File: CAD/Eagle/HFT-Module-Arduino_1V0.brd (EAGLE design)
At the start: 96.5 x 96.5 mm, 402 parts, among them Q0521 ABS07-32.768KHZ, Q0811 ABM03B-32.000MHZ, Q0911 ABM3B-16MHZ-10-R50-1-U, T1201 MMBT2222, T1202 MMBT2222, T1203 MMBT2222, U0111 STM32L4Z_144PIN_SMPS, U0431 PAM2305AAB120, U0601 LM4120IM5-3.0, U0611 MAX5217, U0631 CFPT-141-20MHZ, U0641 OPA354, U0701 Si5338, U0801 SX1276, U0901 AX5243, U0911 PE4259, U0921 PE4259, U0991 PE4259, U1101 MCP3911A0-E-SS, U1111 MAX5136AGTG+, U1121 OPA354, U1131 OPA354, U1141 OPA354, U1201 NHD-C0220BIZ_2X20CHARS, U1301 MPU-9250, U1311 MS5607-02BA03, U1321 SHT31-DIS, U1401 SOLARPANEL_3V3_5MA1_25MM_X_20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, U1402 SPV1040T, U1501 TS5A23166, U1601 SC189ZSKTRT, U1701 TS5A23166, U1801 TS5A23166, U1901 TS5A23166, X1261 TTE_EN11-HSM, X2001 MOLEX 105017-0001, X2101 SMA_SMT_AMPHENOL-901-143, SAM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, X2111 SMA_SMT_AMPHENOL-901-143, SAM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, X2201 CUI SJ1-3535NS, X2211 CUI SJ1-3535NS, X2311 2X20/90_1MM27_HARWIN_M50-3202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, X2312 2X20/90_1MM27_HARWIN_M50-3202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, X2321 2X20/90_1MM27_HARWIN_M50-3202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, X2322 2X20/90_1MM27_HARWIN_M50-3202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, X2331 2X20/90_1MM27_HARWIN_M50-3202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, X2332 2X20/90_1MM27_HARWIN_M50-3202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

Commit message: HW_1V0 - Initial setup of PCB
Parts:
- removed C0313, C0421, C0422, C0432, C0441, C0601, C0611, C0612, C0631, C0641, C0701, C0702, C0703, C0705, C1001, C1002, C1003, C1101, C1102, C1103, C1111, C1112, C1231, C1301, C1303, C1311, C1321, C1402, C1403, C1501, C1605, C1701, C1703, C1801, C1803, C1901, C1902, C1903, C1908, C1909: 100nF, rcl:C0603
- removed C0401, C0402, C0403, C0404, C0405, C0406, C0407, C0408, C0409, C0802, C0803, C0804, C0805, C0806, C0807: 100n, rcl:C0603
- removed C0410, C0423: 4.7uF, rcl:C0805
- removed C0412, C0715, C0716, C1302: 10nF, rcl:C0603
- removed C0413, C0442, C0622, C1211, C1221: 1uF, rcl:C0805
- removed C0431, C0444, C1401, C1404: 10uF, rcl:C0805
- removed C0451, C1601, C1607: 1F_EEC-S5R5H105N, df4iah_rcl:W14MM_D8MM_P13MM5
- removed C0511, C0861: 1.5pF, rcl:C0603
- removed C0531: TZY2Z100AC01R00, df4iah_c-trimm:3MM2_X_2MM5
- removed C0632: 100pF, rcl:C0603
- removed C0704: 220nF, rcl:C0603
- removed C0801: 1u, rcl:C0603
- removed C0811: 4.7p, df4iah_c-trimm:3MM2_X_2MM5
- removed C0812: 4.7p, rcl:C0603
- removed C0841, C0850, C0858, C0872, C_AX_C1, C_AX_C2, C_AX_M2: 0pF, rcl:C0603
- removed C0843: 3.3pF, rcl:C0603
- removed C0844, C0846, C0851, C0852, C0873, C0875, C1113: 47pF, rcl:C0603
- removed C0853, C0863, C0871, C_AX_A2, C_AX_A3, C_AX_B2, C_AX_F2, C_AX_M1: 4.7pF, rcl:C0603
- removed C0854: 15nH, rcl:C0603
- removed C0856, C0859: 6.8pF, rcl:C0603
- removed C0857: 2.7pF, rcl:C0603
- removed C0862: 33pF, rcl:C0603
- removed C0864: 1.2pF, rcl:C0603
- removed C0865: 1.8pF, rcl:C0603
- removed C0911, C0921, C0999, C1261, C1262, C1271: 1nF, rcl:C0603
- removed C0991: 100pF HiQ, rcl:C0603
- removed C0992, C0993: 330pF HiQ, rcl:C0603
- removed C0994, C0996: 0nF HiQ, rcl:C0603
- removed C1104, C1105, C1131, C1141: 220nF, df4iah_rcl:C0603
- removed C1128, C1129: 100nF, df4iah_rcl:C0603
- removed C1132, C1142: 100uF, df4iah_rcl:C0805
- removed C1405: 0nF, rcl:C0603
- removed C1406, C1602, C1606: 47uF, rcl:C0805
- removed C2003: 1nF, df4iah_rcl:C0603
- removed C_AX_T1, C_AX_T2: 4.3pF, rcl:C0603
- removed D0451: CMAD6001, df4iah_diode:SOD923
- removed D1403, D1501: CRS08, df4iah_diode:SOD80C
- removed FM1, FM2, FM3: (no value), df4iah_fiducial:FIDUCIAL_MARK_1MM
- removed H2401, H2404: MOUNT-PAD-ROUND2.8, holes:2,8-PAD
- removed L0411, L1102, L1112: 10uH, rcl:L2012C
- removed L0433: 2.2uH 14mR, df4iah_rcl:L_6X6MM
- removed L0842, L0862: 10nH, rcl:R0603
- removed L0851: 68nH, rcl:R0603
- removed L0856, L0858, L0995, R0201, R0202, R0211, R0212, R0221, R0222, R0231, R0232, R0441, R0612, R0613, R0811, R0845, R0874, R1404, R1405, R1406, R1409: 0R, rcl:R0603
- removed L0857: 12nH, rcl:R0603
- removed L0861: 33nH, rcl:R0603
- removed L0864: 6.2nH, rcl:R0603
- removed L0871: 18nH, rcl:R0603
- removed L1403: 33uH, df4iah_rcl:L_13.5X12.5MM
- removed L1604: 1.0uH 33mR, rcl:L5650M
- removed L_AX_1, L_AX_B1, L_AX_B2, L_AX_F1: 22nH, rcl:R0603
- removed L_AX_C1, L_AX_C2: 100nH, rcl:R0603
- removed L_AX_T1, L_AX_T2: 43nH, rcl:R0603
- removed PF2011: 1.1A/2.2A, rcl:M1206
- removed Q0521: ABS07-32.768KHZ, df4iah_crystal:ABS07
- removed Q0811: ABM03B-32.000MHZ, df4iah_crystal:ABM03B
- removed Q0911: ABM3B-16MHZ-10-R50-1-U, df4iah_crystal:ABM03B
- removed R0241, R0242, R0243, R0251, R0252, R0253, R0254, R0261, R0262, R0263, R0269, R0271, R0272, R0273, R0274, R0275, R0276, R0277, R0281, R0282, R0283, R0284, R0285, R0286, R0287, R0288, R0289, R0290, R0291, R0292, R0293, R0294, R0295, R0296, R0642, R0713, R0714, R0723, R0724, R0731, R0732, R0735, R0736, R0743, R0744, R0802, R0803, R0831, R1021, R1041, R1051, R1061, R1106, R1107, R1108, R1109, R1114, R2310, R2311, R2312, R2313, R2314, R2315, R2316, R2317, R2318, R2320, R2321, R2322, R2323, R2324, R2325, R2326, R2327, R2328, R2330, R2331, R2332, R2333, R2334, R2335, R2336, R2337, R2338: 47R, rcl:R0603
- removed R0311: 3.3kR, rcl:R0603
- removed R0321, R0631, R1131, R1141, R1261, R1262, R1271: 10kR, rcl:R0603
- removed R0611: open, rcl:R0603
- removed R0621, R1031, R1032, R1407, R1412: 100kR, rcl:R0603
- removed R0638, R0639: 50R, rcl:R0603
- removed R0711, R0712: none, rcl:R0603
- removed R0751, R0801, R0821: 100R, rcl:R0603
- removed R0804, R0805, R0806, R0807: NC, rcl:R0603
- removed R1104, R1105: 22kR, rcl:R0603
- removed R1110, R1132, R1135, R1142, R1145, R1241, R1502, R1702, R1802, R1902: 33kR, rcl:R0603
- removed R1201, R1205, R1208: 1.8kR, rcl:R0603
- removed R1202: 5.2kR, rcl:R0603
- removed R1203: 68R, rcl:R0805
- removed R1204, R1207: 2.2kR, rcl:R0603
- removed R1206, R1209: 10R, rcl:R0805
- removed R1301: 68R, rcl:R0603
- removed R1331, R1332: 3.9kR, rcl:R0603
- removed R1408: 310kR, rcl:R0603
- removed R1411: 1kR, rcl:R0603
- removed R2002: 330kR, rcl:R0603
- removed S0312: KSR223G, df4iah_switch:KSR223G_SMD_1POL
- removed SJ0121, SJ0401, SJ0421, SJ0422, SJ0423, SJ0424: (no value), df4iah_jumper:SJ
- removed T1201, T1202, T1203: MMBT2222, transistor:SOT23
- removed TP_+1V2, TP_+1V2_MCU, TP_+3V3, TP_+3V3_20MHZ, TP_+3V3_HICUR, TP_+5V0, TP_+5V0_SOL, TP_+5V0_USB_SW, TP_VBAT, TP_VSOL: PTR1B1,27, testpad:B1,27
- removed TP_AX_ADC1, TP_AX_ADC2, TP_AX_IRQ, TP_AX_TCXO_EN, TP_SX_DIO0, TP_SX_DIO1, TP_SX_DIO2, TP_SX_DIO3, TP_SX_DIO4, TP_SX_DIO5, TP_SX_RXTX: PTR1TP06R, testpad:TP06R
- removed U0111: STM32L4Z_144PIN_SMPS, df4iah_stm32l4:LQFP144
- removed U0431: PAM2305AAB120, df4iah_powersupply:SOT95P280X145-5N
- removed U0601: LM4120IM5-3.0, df4iah_powersupply:SOT95P285X120-5N
- removed U0611: MAX5217, df4iah_dac:µMAX8
- removed U0631: CFPT-141-20MHZ, df4iah_osc:CFPT-141
- removed U0641, U1121, U1131, U1141: OPA354, df4iah_opamp:SOT-23-5
- removed U0701: Si5338, df4iah_osc:QFN24_P0MM5_CTRPAD
- removed U0801: SX1276, df4iah_rf:QFN28-6X6-0P65-PAD
- removed U0901: AX5243, df4iah_rf:QFN20-4X4-0P5-PAD
- removed U0911, U0921, U0991: PE4259, df4iah_rf:SC-70_6-LEAD_2X1MM25_0P65
- removed U1101: MCP3911A0-E-SS, df4iah_adc:QFN20_P0MM5_CTRPAD
- removed U1111: MAX5136AGTG+, df4iah_dac:QFN24_P0MM5_CTRPAD
- removed U1201: NHD-C0220BIZ_2X20CHARS, df4iah_lcd:NHD-C0220BIZ_2X20CHARS
- removed U1301: MPU-9250, df4iah_sensors:QFN24-3X3
- removed U1311: MS5607-02BA03, df4iah_sensors:MS5607-02BA
- removed U1321: SHT31-DIS, df4iah_sensors:DFN8/SHT
- removed U1401: SOLARPANEL_3V3_5MA1_25MM_X_20MM, df4iah_supply:SOLARPANEL_3V3_5MA1_25MM_X_20MM
- removed U1402: SPV1040T, df4iah_powersupply:TSSOP8
- removed U1501, U1701, U1801, U1901: TS5A23166, df4iah_sc-switches:R-PDSO-G8
- removed U1601: SC189ZSKTRT, df4iah_powersupply:SOT95P280X145-5N
- removed X0301: (no value), df4iah_connector:2X03
- removed X0322: (no value), df4iah_connector:1X02
- removed X1261: TTE_EN11-HSM, df4iah_switch:TTE_EN11-HSM
- removed X2001: MOLEX 105017-0001, df4iah_connector:USB-B-MICRO-SMD_MOLEX-105017-0001
- removed X2101, X2111: SMA_SMT_AMPHENOL-901-143, SAMTEC SMA-J-P-H-RA-TH1, df4iah_connector:SMA_SMT_AMPHENOL_901-143
- removed X2201, X2211: CUI SJ1-3535NS, df4iah_connector:SJ1-353XNS_3MM5-STEREO-AUDIO-JACKS
- removed X2311, X2312, X2321, X2322, X2331, X2332: 2X20/90_1MM27_HARWIN_M50-3202045, df4iah_connector:2X20/90_1MM27_HARWIN_M50-3202045
- added R111, R112, R113, R114, R115, R121, R122, R123, R124: 47R, rcl:R0603
- added X111, X121: 2X20/90_1MM27_HARWIN_M50-3202045, df4iah_connector:2X20/90_1MM27_HARWIN_M50-3202045
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- renumbered H2402 to H412, H2403 to H411
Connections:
- removed net +1V2: C0444.1, C1901.1, L0433.1, TP_+1V2.TP, U0431.4, U1901.1, U1901.5
- removed net +1V5_UNUSED: SJ0424.2
- removed net +1V8_UNUSED: SJ0423.2
- removed net +2V5_UNUSED: SJ0422.2
- removed net +3V0_20MHZ_VCTCXO: C0611.1, C0631.1, U0601.5, U0611.1, U0631.4
- removed net +3V3_20MHZ: C0612.1, C0641.1, C1803.1, R0611.1, R0613.1, TP_+3V3_20MHZ.TP, U0611.7, U0641.5, U1801.2, U1801.6
- removed net +3V3_HICUR: C0701.1, C0702.1, C0703.1, C0704.1, C0705.2, C1101.1, C1111.1, C1128.1, C1129.1, C1703.1, L1102.2, L1112.2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
- removed net +5V1_SOL: C1406.1, R1405.2, R1406.2, R1408.2, R1409.1, TP_+5V0_SOL.TP
- removed net 20MHZ_DAC_OUT: R0621.1, U0611.6
- removed net 20MHZ_XO: R0638.1, U0631.3
- removed net 20MHZ_XON: C0716.1, R0639.2, R0751.1
- removed net 20MHZ_XOP: C0715.1, R0638.2, R0751.2
- removed net AD_VCTCXO1: R0642.1, U0641.1, U0641.4
- removed net AUDIO_IN_L: C1104.1, X2201.2
- removed net AUDIO_IN_R: C1105.1, X2201.3
- removed net AUDIO_OUT_L: C1132.2, X2211.2
- removed net AUDIO_OUT_L_OP: C1132.1, U1131.1, U1131.4
- removed net AUDIO_OUT_R: C1142.2, X2211.3
- removed net AUDIO_OUT_R_OP: C1142.1, U1141.1, U1141.4
- removed net AX_16MHZ: R0714.1, R1021.2
- removed net AX_ADC1: R1031.1, TP_AX_ADC1.TP, U0901.17
- removed net AX_ADC2: R1032.1, TP_AX_ADC2.TP, U0901.18
- removed net AX_ANTN: C_AX_C2.1, C_AX_T2.1, L_AX_C2.1, U0901.4
- removed net AX_ANTP: C_AX_C1.1, C_AX_T1.1, L_AX_C1.1, U0901.3
- removed net AX_B1: C_AX_M1.1, L_AX_B1.1, L_AX_T1.2
- removed net AX_B2: C_AX_B2.1, C_AX_M2.1, L_AX_B2.2, L_AX_T2.2
- removed net AX_CLK16N: Q0911.1, U0901.19
- removed net AX_CLK16P: Q0911.3, U0901.20
- removed net AX_COMB: C_AX_A2.1, C_AX_B2.2, C_AX_F2.1, L_AX_B1.2, L_AX_F1.1
- removed net AX_GPIO1: R1061.2, TP_AX_TCXO_EN.TP, U0901.15
- removed net AX_IRQ: R1051.2, TP_AX_IRQ.TP, U0901.14
- removed net AX_L1: L_AX_1.1, U0901.8
- removed net AX_L2: L_AX_1.2, U0901.7
- removed net AX_SYSCLK: R1021.1, U0901.9
- removed net AX_T1: C_AX_T1.2, L_AX_T1.1
- removed net AX_T2: C_AX_T2.2, L_AX_T2.1
- removed net AX_VDD1: C1002.2, U0901.1
- removed net AX_VDD5: C1003.2, U0901.5
- removed net CH1_ANT: C0996.1, L0995.2, X2101.1
- removed net CH2_ANT: C_AX_A3.1, C_AX_F2.2, L_AX_F1.2, X2111.1
- removed net CLK0_N: R0743.2, X2332.4
- removed net CLK0_P: R0744.2, X2332.3
- removed net CLK1_N: R0735.2, X2322.4
- removed net CLK1_P: R0736.2, X2322.3
- removed net CLK2_N: R0731.2, X2312.4
- removed net CLK2_P: R0732.2, X2312.3
- removed net EVT_N: R2314.2, X2311.29
- removed net EVT_S: R2334.2, X2331.29
- removed net EVT_W: R2324.2, X2321.29
- removed net I2S_FS_IN_N: R2317.2, X2312.26
- removed net I2S_FS_IN_S: R2337.2, X2332.26
- removed net I2S_FS_IN_W: R2327.2, X2322.26
- removed net I2S_FS_OUT: R0284.2, X2312.20, X2322.20, X2332.20
- removed net I2S_MCLK_OUT: R0283.2, X2312.19, X2322.19, X2332.19
- removed net I2S_SCK_IN_N: R2315.2, X2312.23
- removed net I2S_SCK_IN_S: R2335.2, X2332.23
- removed net I2S_SCK_IN_W: R2325.2, X2322.23
- removed net I2S_SCK_OUT: R0281.2, X2312.17, X2322.17, X2332.17
- removed net I2S_SD_IN_N: R2316.2, X2312.24
- removed net I2S_SD_IN_S: R2336.2, X2332.24
- removed net I2S_SD_IN_W: R2326.2, X2322.24
- removed net I2S_SD_OUT: R0282.2, X2312.18, X2322.18, X2332.18
- removed net LCD_C1+: C1211.2, U1201.7
- removed net LCD_C1-: C1211.1, U1201.8
- removed net LCD_VOUT: C1221.1, U1201.6
- removed net LED_B_B: R1207.1, R1208.2, T1203.1
- removed net LED_B_E: R1209.2, T1203.2
- removed net LED_B_K: T1203.3, U1201.11
- removed net LED_G_B: R1204.1, R1205.2, T1202.1
- removed net LED_G_E: R1206.2, T1202.2
- removed net LED_G_K: T1202.3, U1201.10
- removed net LED_R_B: R1201.1, R1202.2, T1201.1
- removed net LED_R_E: R1203.2, T1201.2
- removed net LED_R_K: T1201.3, U1201.9
- removed net MAX5136_!READY: R1114.2, U1111.4
- removed net MAX5136_AVDD: C1112.2, L1112.1, U1111.16, U1111.24
- removed net MAX5136_OUT0: R1131.1, U1111.1
- removed net MAX5136_OUT0_R: C1131.1, R1131.2
- removed net MAX5136_OUT0_SUM: C1131.2, R1132.2, R1135.2, U1131.3
- removed net MAX5136_OUT1: R1141.1, U1111.18
- removed net MAX5136_OUT1_R: C1141.1, R1141.2
- removed net MAX5136_OUT1_SUM: C1141.2, R1142.2, R1145.2, U1141.3
- removed net MAX5136_REF: C1113.1, U1111.21, U1111.22, U1121.3
- removed net MAX5136_REF_OP: R1132.1, R1142.1, U1121.1, U1121.4
- removed net MAX5217_!AUX: R0613.2, U0611.5
- removed net MAX5217_ADDR: R0611.2, R0612.2, U0611.2
- removed net MCP3911_!DR: R1106.1, U1101.11
- removed net MCP3911_CH0+: C1104.2, R1104.2, U1101.1
- removed net MCP3911_CH1+: C1105.2, R1105.2, U1101.3
- removed net MCP3911_MDAT0: R1108.1, U1101.10
- removed net MCP3911_MDAT1: R1109.1, U1101.9
- removed net MCP3911_REFINOUT: C1103.2, U1101.6
- removed net MCP3911_SDO: R1107.1, U1101.16
- removed net MCU_AX_MISO: R1041.2, U0901.12
- removed net MCU_I2C1_SCL: R0201.2, X2312.7
- removed net MCU_I2C1_SDA: R0202.2, X2312.8
- removed net MCU_I2C2_SCL: R0211.2, X2322.7
- removed net MCU_I2C2_SDA: R0212.2, X2322.8
- removed net MCU_I2C3_SCL: R0221.2, X2332.7
- removed net MCU_I2C3_SDA: R0222.2, X2332.8
- removed net MCU_I2C4_SCL: R0231.2, R1332.1, U0611.3, U0701.12, U1201.2, U1301.23, U1311.8, U1321.4
- removed net MCU_I2C4_SDA: R0232.2, R1331.1, U0611.4, U0701.19, U1201.3, U1301.24, U1311.7, U1321.1
- removed net MCU_MCO: R0271.2, R0713.1
- removed net MCU_NRST: C0313.1, R0311.2, S0312.2, U0111.25
- removed net MCU_OUT_20MHZ_EN: R0273.2, R1802.2, U0601.3, U1801.3, U1801.7
- removed net MCU_OUT_AUDIO_ADC_NRESET: R0261.2, R1110.2, U1101.18
- removed net MCU_OUT_AUDIO_ADC_SEL: R0262.2, U1101.14
- removed net MCU_OUT_AUDIO_DAC_SEL: R0263.2, U1111.10
- removed net MCU_OUT_AX_SEL: R0253.2, U0901.10
- removed net MCU_OUT_HICUR_EN: R0275.2, R1702.2, U1701.3, U1701.7
- removed net MCU_OUT_LCD_NRST: R0272.2, R1241.2, U1201.1
- removed net MCU_OUT_SX_SEL: R0254.2, U0801.19
- removed net MCU_OUT_VDD12_EN: R0276.2, R1902.2, U1901.3, U1901.7
- removed net MCU_OUT_VUSB_EN: R0274.2, R1502.2, U1501.3, U1501.7
- removed net MCU_SPI1_MISO: R0243.2, X2312.12, X2322.12, X2332.12
- removed net MCU_SPI1_MOSI: R0242.2, X2312.11, X2322.11, X2332.11
- removed net MCU_SPI1_SCK: R0241.2, X2312.13, X2322.13, X2332.13
- removed net MCU_SPI3_MOSI: R0252.2, U0801.18, U0901.13, U1101.17, U1111.9
- removed net MCU_SPI3_SCK: R0251.2, U0801.16, U0901.11, U1101.15, U1111.12
- removed net MCU_SX_TX_RX_CTRL: R0277.2, U0991.4
- removed net MCU_VBAT: C0451.+, D0451.C, TP_VBAT.TP, U0111.6
- removed net MCU_VDD: C0401.1, C0402.1, C0403.1, C0404.1, C0405.1, C0406.1, C0407.1, C0408.1, C0409.1, C0410.1, L0411.2, SJ0401.2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
- removed net MCU_VDD12: C1903.1, C1908.2, C1909.1, TP_+1V2_MCU.TP, U0111.142, U0111.70, U1901.2, U1901.6
- removed net MCU_VDDA: C0412.1, C0413.1, L0411.1, U0111.33
- removed net MCU_VDDIO2: C0421.2, C0422.1, C0423.1, SJ0421.1, SJ0422.1, SJ0423.1, SJ0424.1, U0111.131, U0111.95
- removed net MCU_VREF_M: R0441.2, U0111.31
- removed net MCU_VREF_P: C0441.2, C0442.2, U0111.32
- removed net MCU_VSSA: SJ0121.2, U0111.30
- removed net MCU_WAKEUP: R0269.2, X2311.33, X2321.33, X2331.33
- removed net MPU_INT: R1301.1, U1301.12
- removed net MPU_REGOUT: C1303.1, U1301.10
- removed net MVP3911_AVDD: C1102.2, L1102.1, U1101.20
- removed net PA0: R0292.1, U0111.34
- removed net PA1: U0111.35
- removed net PA10: U0111.102, X2001.ID
- removed net PA13: U0111.105, X0301.1
- removed net PA14: U0111.109, X0301.5
- removed net PA15: U0111.110
- removed net PA2: R0289.1, U0111.36
- removed net PA3: R1411.2, U0111.37
- removed net PA4: U0111.40
- removed net PA5: U0111.41
- removed net PA6: R0296.1, U0111.42
- removed net PA7: R1204.2, U0111.43
- removed net PA8: R0271.1, U0111.100
- removed net PA9: PF2011.1, U0111.101, X2001.VBUS
- removed net PA_USB_N: U0111.103, X2001.D-
- removed net PA_USB_P: U0111.104, X2001.D+
- removed net PB0: R1207.2, U0111.46
- removed net PB1: R0295.1, U0111.47
- removed net PB10: R1261.2, U0111.69
- removed net PB12: R1262.2, U0111.73
- removed net PB13: R2315.1, R2325.1, R2335.1, U0111.74
- removed net PB14: R1271.2, U0111.75
- removed net PB15: U0111.76
- removed net PB2: U0111.48
- removed net PB3: R2310.1, U0111.132
- removed net PB4: U0111.133
- removed net PB5: R2311.1, U0111.134
- removed net PB6: R2312.1, U0111.135
- removed net PB7: R2313.1, U0111.136
- removed net PB8: U0111.138
- removed net PB9: U0111.139
- removed net PC0: R0276.1, U0111.26
- removed net PC1: R0275.1, U0111.27
- removed net PC10: R0251.1, U0111.111
- removed net PC11: R0831.1, R1041.1, R1107.2, U0111.112
- removed net PC12: R0252.1, U0111.113
- removed net PC13: R0269.1, U0111.7
- removed net PC14_MCU_OSC32_IN: C0531.-, Q0521.2, U0111.8
- removed net PC15_MCU_OSC32_OUT: C0511.1, Q0521.1, U0111.9
- removed net PC2: R0274.1, U0111.28
- removed net PC3: R0273.1, U0111.29
- removed net PC4: R0293.1, U0111.44
- removed net PC5: R0294.1, U0111.45
- removed net PC6: R1201.2, U0111.96
- removed net PC7: U0111.97
- removed net PC8: R1114.1, U0111.98
- removed net PC9: R0263.1, U0111.99
- removed net PD0: R1109.2, U0111.114
- removed net PD1: R1108.2, U0111.115
- removed net PD10: R2331.1, U0111.79
- removed net PD11: R2316.1, R2326.1, R2336.1, U0111.80
- removed net PD12: R2317.1, R2327.1, R2337.1, U0111.81
- removed net PD13: R0232.1, U0111.82
- removed net PD14: R2332.1, U0111.85
- removed net PD15: R2333.1, U0111.86
- removed net PD2: R1106.2, U0111.116
- removed net PD3: R0261.1, U0111.117
- removed net PD4: R0291.1, U0111.118
- removed net PD5: R0262.1, U0111.119
- removed net PD6: R0290.1, U0111.122
- removed net PD7: U0111.123, U0701.8
- removed net PD8: R0821.1, U0111.77
- removed net PD9: R2330.1, U0111.78
- removed net PE0: R2314.1, U0111.140
- removed net PE1: U0111.141
- removed net PE10: R0283.1, U0111.63
- removed net PE11: R0253.1, U0111.64
- removed net PE12: R0254.1, U0111.65
- removed net PE13: R0241.1, U0111.66
- removed net PE14: R0243.1, U0111.67
- removed net PE15: R0242.1, U0111.68
- removed net PE2: R2323.1, U0111.1
- removed net PE3: R0282.1, U0111.2
- removed net PE4: R2322.1, U0111.3
- removed net PE5: R2321.1, U0111.4
- removed net PE6: U0111.5
- removed net PE7: R1051.1, U0111.58
- removed net PE8: R0281.1, U0111.59
- removed net PE9: R0284.1, U0111.60
- removed net PF0: R0212.1, U0111.10
- removed net PF1: R0211.1, U0111.11
- removed net PF10: R2324.1, U0111.22
- removed net PF11: U0111.49
- removed net PF12: R0272.1, U0111.50
- removed net PF13: R1301.2, U0111.53
- removed net PF14: R0231.1, U0111.54
- removed net PF15: U0111.55
- removed net PF2: R2320.1, U0111.12
- removed net PF3: R0642.2, U0111.13
- removed net PF4: U0111.14
- removed net PF5: U0111.15
- removed net PF6: R2318.1, U0111.18
- removed net PF7: R2328.1, U0111.19
- removed net PF8: R2338.1, U0111.20
- removed net PF9: R1412.1, U0111.21
- removed net PG0: R0277.1, U0111.56
- removed net PG1: R1061.1, U0111.57
- removed net PG10: R0286.1, U0111.125
- removed net PG11: R0288.1, U0111.126
- removed net PG12: R0287.1, U0111.127
- removed net PG13: R0202.1, U0111.128
- removed net PG14: R0201.1, U0111.129
- removed net PG2: R0802.2, U0111.87
- removed net PG3: R0803.2, U0111.88
- removed net PG4: R2334.1, U0111.89
- removed net PG5: U0111.90
- removed net PG6: U0111.91
- removed net PG7: R0221.1, U0111.92
- removed net PG8: R0222.1, U0111.93
- removed net PG9: R0285.1, U0111.124
- removed net PH0: R0724.1, U0111.23
- removed net PH1: U0111.24
- removed net PH3_BOOT0: R0321.2, U0111.137, X0322.1
- removed net PN00: R2310.2, X2311.7
- removed net PN01: R2311.2, X2311.9
- removed net PN02: R2312.2, X2311.11
- removed net PN03: R2313.2, X2311.13
- removed net PS00: R2330.2, X2331.7
- removed net PS01: R2331.2, X2331.9
- removed net PS02: R2332.2, X2331.11
- removed net PS03: R2333.2, X2331.13
- removed net PW00: R2320.2, X2321.7
- removed net PW01: R2321.2, X2321.9
- removed net PW02: R2322.2, X2321.11
- removed net PW03: R2323.2, X2321.13
- removed net ROTENC_A: C1261.1, R1261.1, X1261.A
- removed net ROTENC_B: C1262.1, R1262.1, X1261.B
- removed net ROTENC_E: C1271.1, R1271.1, X1261.E
- removed net SI5338_CLK0A: R0744.1, U0701.22
- removed net SI5338_CLK0B: R0743.1, U0701.21
- removed net SI5338_CLK1A: R0736.1, U0701.18
- removed net SI5338_CLK1B: R0735.1, U0701.17
- removed net SI5338_CLK2A: R0732.1, U0701.14
- removed net SI5338_CLK2B: R0731.1, U0701.13
- removed net SI5338_CLK3A: R0724.2, U0701.10
- removed net SI5338_CLK3B: R0723.2, U0701.9
- removed net SI5338_CLK3B_2: R0723.1, U1101.12
- removed net SI5338_IN1: R0711.2, U0701.1
- removed net SI5338_IN2: R0712.2, U0701.2
- removed net SI5338_IN3: R0713.2, U0701.3
- removed net SI5338_IN4: R0714.2, U0701.4
- removed net SI5338_IN5: C0715.2, U0701.5
- removed net SI5338_IN6: C0716.2, U0701.6
- removed net SI5338_IN_CLK1: R0711.1
- removed net SI5338_IN_CLK2: R0712.1
- removed net SPV_ICTRL_M: C1405.2, R1405.1, U1402.6
- removed net SPV_ICTRL_P: C1405.1, R1404.1, U1402.7
- removed net SPV_LX: D1403.A, L1403.1, R1412.2, U1402.3
- removed net SPV_VCTRL: R1407.2, R1408.1, U1402.5
- removed net SPV_VOUT: C1403.1, C1404.1, D1403.C, R1404.2, R1406.1, U1402.4
- removed net SW: L1604.2, U1601.5
- removed net SX_ANT_1: C0993.1, U0991.5
- removed net SX_ANT_2: C0993.2, C0994.1, L0995.1
- removed net SX_DIO0: R0802.1, TP_SX_DIO0.TP, U0801.8
- removed net SX_DIO1: R0803.1, TP_SX_DIO1.TP, U0801.9
- removed net SX_DIO2: R0804.1, TP_SX_DIO2.TP, U0801.10
- removed net SX_DIO2_2: R0804.2
- removed net SX_DIO3: R0805.1, TP_SX_DIO3.TP, U0801.11
- removed net SX_DIO3_2: R0805.2
- removed net SX_DIO4: R0806.1, TP_SX_DIO4.TP, U0801.12
- removed net SX_DIO4_2: R0806.2
- removed net SX_DIO5: R0807.1, TP_SX_DIO5.TP, U0801.13
- removed net SX_DIO5_2: R0807.2
- removed net SX_HF_1: C0991.1, U0911.5
- removed net SX_HF_2: C0991.2, U0991.1
- removed net SX_LF_1: C0992.1, U0921.5
- removed net SX_LF_2: C0992.2, U0991.3
- removed net SX_MISO: R0831.2, U0801.17
- removed net SX_NRESET: R0821.2, U0801.7
- removed net SX_RFI_HF: C0841.1, L0842.1, U0801.21
- removed net SX_RFI_HF_2: C0843.1, C0844.1, L0842.2
- removed net SX_RFI_HF_3: C0844.2, R0845.1
- removed net SX_RFI_HF_4: C0846.1, R0845.2
- removed net SX_RFI_HF_5: C0846.2, U0911.3
- removed net SX_RFI_LF: C0871.1, L0871.1, U0801.1
- removed net SX_RFI_LF_2: C0871.2, C0872.2, C0873.1
- removed net SX_RFI_LF_3: C0873.2, R0874.1
- removed net SX_RFI_LF_4: C0875.1, R0874.2
- removed net SX_RFI_LF_5: C0875.2, U0921.3
- removed net SX_RFO_HF: C0861.1, C0862.1, L0861.1, U0801.22
- removed net SX_RFO_HF_2: C0862.2, L0862.1
- removed net SX_RFO_HF_3: C0863.1, C0864.1, L0862.2, L0864.1
- removed net SX_RFO_HF_4: C0864.2, C0865.1, L0864.2, U0911.1
- removed net SX_RFO_LF: C0853.1, C0854.1, L0851.1, U0801.28
- removed net SX_RFO_LF_2: C0854.2, L0856.1
- removed net SX_RFO_LF_3: C0856.1, C0857.1, L0856.2, L0857.1
- removed net SX_RFO_LF_4: C0857.2, C0858.1, C0859.1, L0857.2, L0858.1
- removed net SX_RFO_LF_5: C0850.1, C0858.2, L0858.2, U0921.1
- removed net SX_RXTX: R0801.1, TP_SX_RXTX.TP, U0801.20
- removed net SX_RXTX_2: R0801.2, U0911.4, U0921.4
- removed net SX_VR_ANA: C0806.2, U0801.2
- removed net SX_VR_DIG: C0807.2, U0801.4
- removed net SX_VR_PA: C0805.2, C0851.1, C0852.1, L0851.2, L0861.2, U0801.25
- removed net SX_XTA: C0811.-, Q0811.1, U0801.5
- removed net SX_XTB: R0811.1, U0801.6
- removed net SX_XTB_R: C0812.2, Q0811.3, R0811.2
- removed net TIMCAP_N: R2318.2, X2311.31
- removed net TIMCAP_S: R2338.2, X2331.31
- removed net TIMCAP_W: R2328.2, X2321.31
- removed net UART1_CTS_IN: R0288.2, X2311.26
- removed net UART1_RTS_OUT: R0287.2, X2311.25
- removed net UART1_RX_IN: R0286.2, X2311.24
- removed net UART1_TX_OUT: R0285.2, X2311.23
- removed net UART2_CTS_IN: R0292.2, X2321.26
- removed net UART2_RTS_OUT: R0291.2, X2321.25
- removed net UART2_RX_IN: R0290.2, X2321.24
- removed net UART2_TX_OUT: R0289.2, X2321.23
- removed net UART3_CTS_IN: R0296.2, X2331.26
- removed net UART3_RTS_OUT: R0295.2, X2331.25
- removed net UART3_RX_IN: R0294.2, X2331.24
- removed net UART3_TX_OUT: R0293.2, X2331.23
- removed net USB_SHIELD: C2003.2, R2002.2, X2001.JSHIELD, X2001.JSHIELD@2, X2001.JSHIELD@3, X2001.JSHIELD@4, X2001.JSHIELD@5, X2001.JSHIELD@6
- removed net VDD12_SW: L0433.2, U0431.5
- removed net VDDUSB: C1501.1, PF2011.2, U1501.1, U1501.5, U1501.8
- removed net VSOL: C1401.1, C1402.1, L1403.2, R1411.1, TP_VSOL.TP, U1401.+VSOL, U1402.1, U1402.8
- removed net VUSB_SW: D1501.A, TP_+5V0_USB_SW.TP, U1501.2, U1501.6
- removed net XO_LP: C0622.1, R0621.2, R0631.1, U0641.3
- removed net XO_VC: C0632.1, R0631.2, U0631.1
- new net EXP_CLK_IN_N: X111.38
- new net EXP_CLK_IN_P: X111.37
- new net EXP_EVENT_IN: X121.11
- new net EXP_I2C_SCL_IN: X111.33
- new net EXP_I2C_SDA_INOUT: X111.34
- new net EXP_I2S_MSR_FS_OUT: R112.1
- new net EXP_I2S_MSR_FS_OUT_R: R112.2, X111.16
- new net EXP_I2S_MSR_MCLK_OUT: R111.1
- new net EXP_I2S_MSR_MCLK_OUT_R: R111.2, X111.15
- new net EXP_I2S_MSR_SCK_OUT: R113.1
- new net EXP_I2S_MSR_SCK_OUT_R: R113.2, X111.17
- new net EXP_I2S_MSR_SD_OUT: R114.1
- new net EXP_I2S_MSR_SD_OUT_R: R114.2, X111.18
- new net EXP_I2S_SLV_FS_IN: X111.22
- new net EXP_I2S_SLV_MCLK_IN: X111.21
- new net EXP_I2S_SLV_SCK_IN: X111.23
- new net EXP_I2S_SLV_SD_IN: X111.24
- new net EXP_PX0_INOUT: X121.33
- new net EXP_PX1__INOUT: X121.31
- new net EXP_PX2_INOUT: X121.29
- new net EXP_PX3_INOUT: X121.27
- new net EXP_SPI_MISO_OUT: R115.1
- new net EXP_SPI_MISO_OUT_R: R115.2, X111.30
- new net EXP_SPI_MOSI_IN: X111.29
- new net EXP_SPI_SCK_IN: X111.27
- new net EXP_TMRCAPT_OUT: R122.1
- new net EXP_TMRCAPT_OUT_R: R122.2, X121.9
- new net EXP_UART_CTS_IN: X121.15
- new net EXP_UART_RTS_OUT: R123.1
- new net EXP_UART_RTS_OUT_R: R123.2, X121.16
- new net EXP_UART_RX_IN: X121.17
- new net EXP_UART_TX_OUT: R124.1
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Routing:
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- removed copper zone on layer 15, net +3V3
- removed copper zone on layer 1, net GND
- removed copper zone on layer 16, net GND
- removed copper zone on layer 2, net GND
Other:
- board text added: "2x 2.8 mm"
- board text added: "HFT-Module-Arduino V1.0 (C) 2018 by HFT-Institut, Hochschule Mannheim, Germany"
- board text added: "Position Archer-Headers in mil: TOP x: 3800 - 200, y: 2450 BOT x: 3800 - 200, y: 1300"
- board text removed: "+5V1_SOL"
- board text removed: "1.2V"
- board text removed: "3.3V"
- board text removed: "4x 2.8 mm"
- board text removed: "5V"
- board text removed: "ADC1"
- board text removed: "ADC2"
- board text removed: "GPIO"
- board text removed: "HFT-Core-Module V1.0 (C) 2018 by HFT-Institut, Hochschule Mannheim, Germany"
- board text removed: "HI"
- board text removed: "IN"
- board text removed: "IRQ"
- board text removed: "OUT"
- board text removed: "RESET"
- board text removed: "Solar panel"
- board text removed: "USB"
- board text removed: "VBAT"
- board text removed: "VSOL"
- board text removed: "XO"

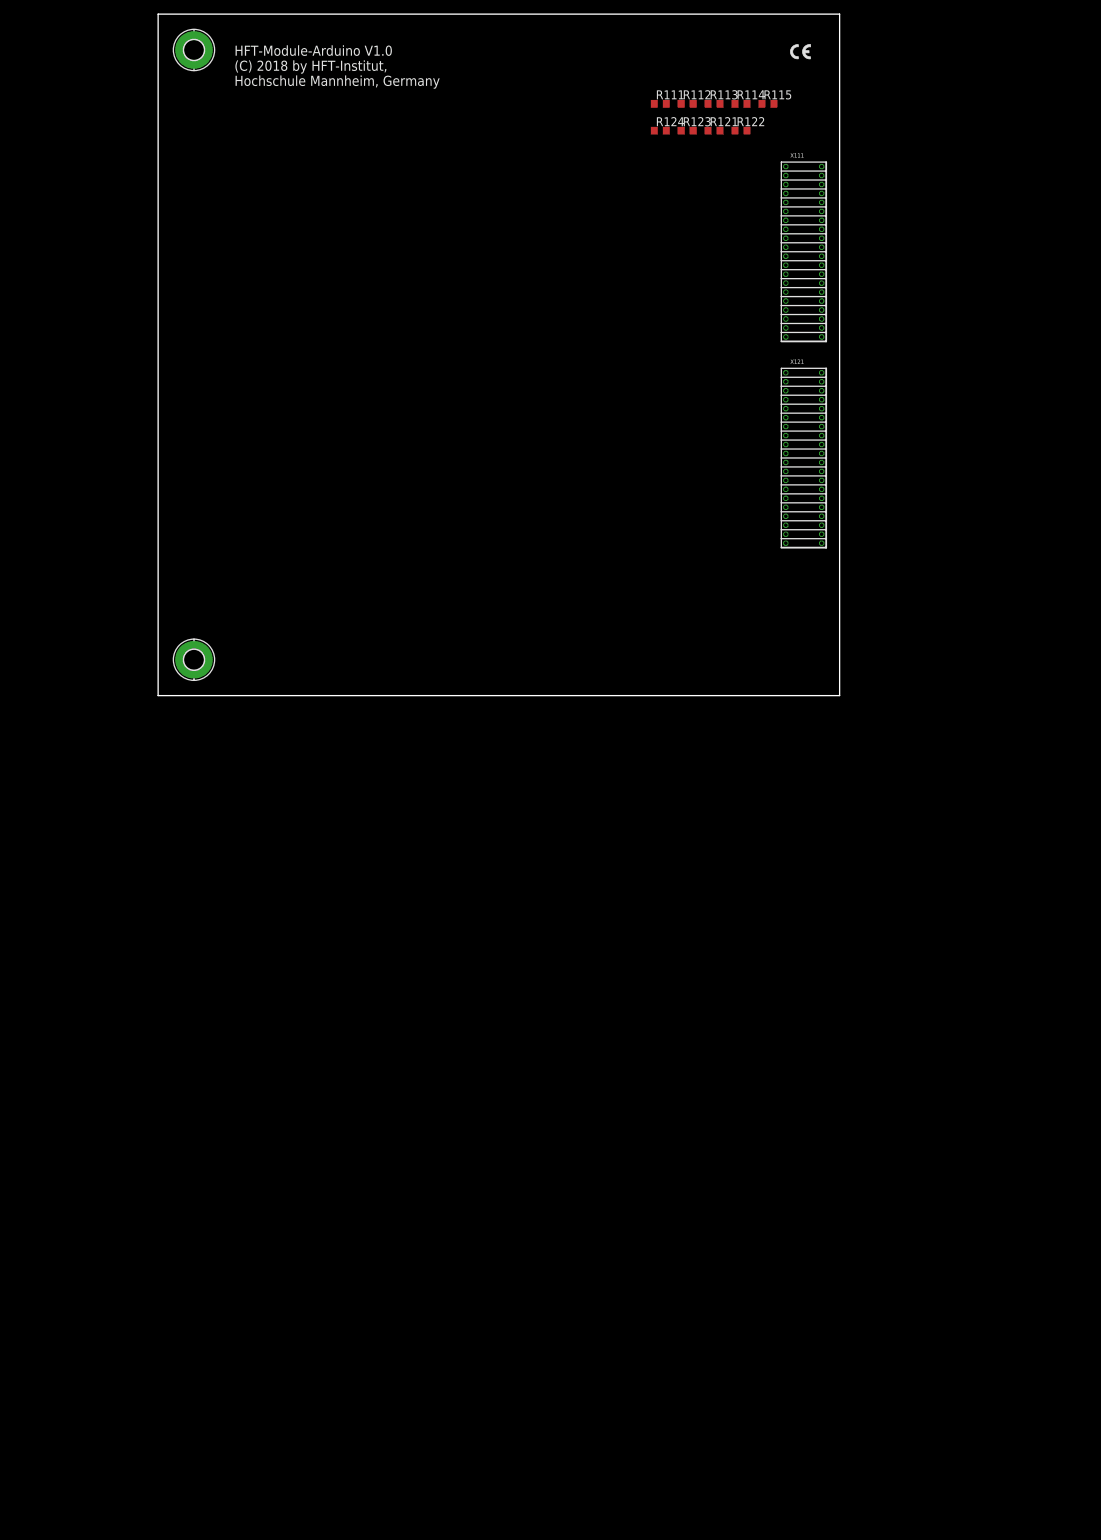
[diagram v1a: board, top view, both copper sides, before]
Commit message: HW_1V0 - CAD/Eagle - Arduino compatible headers added
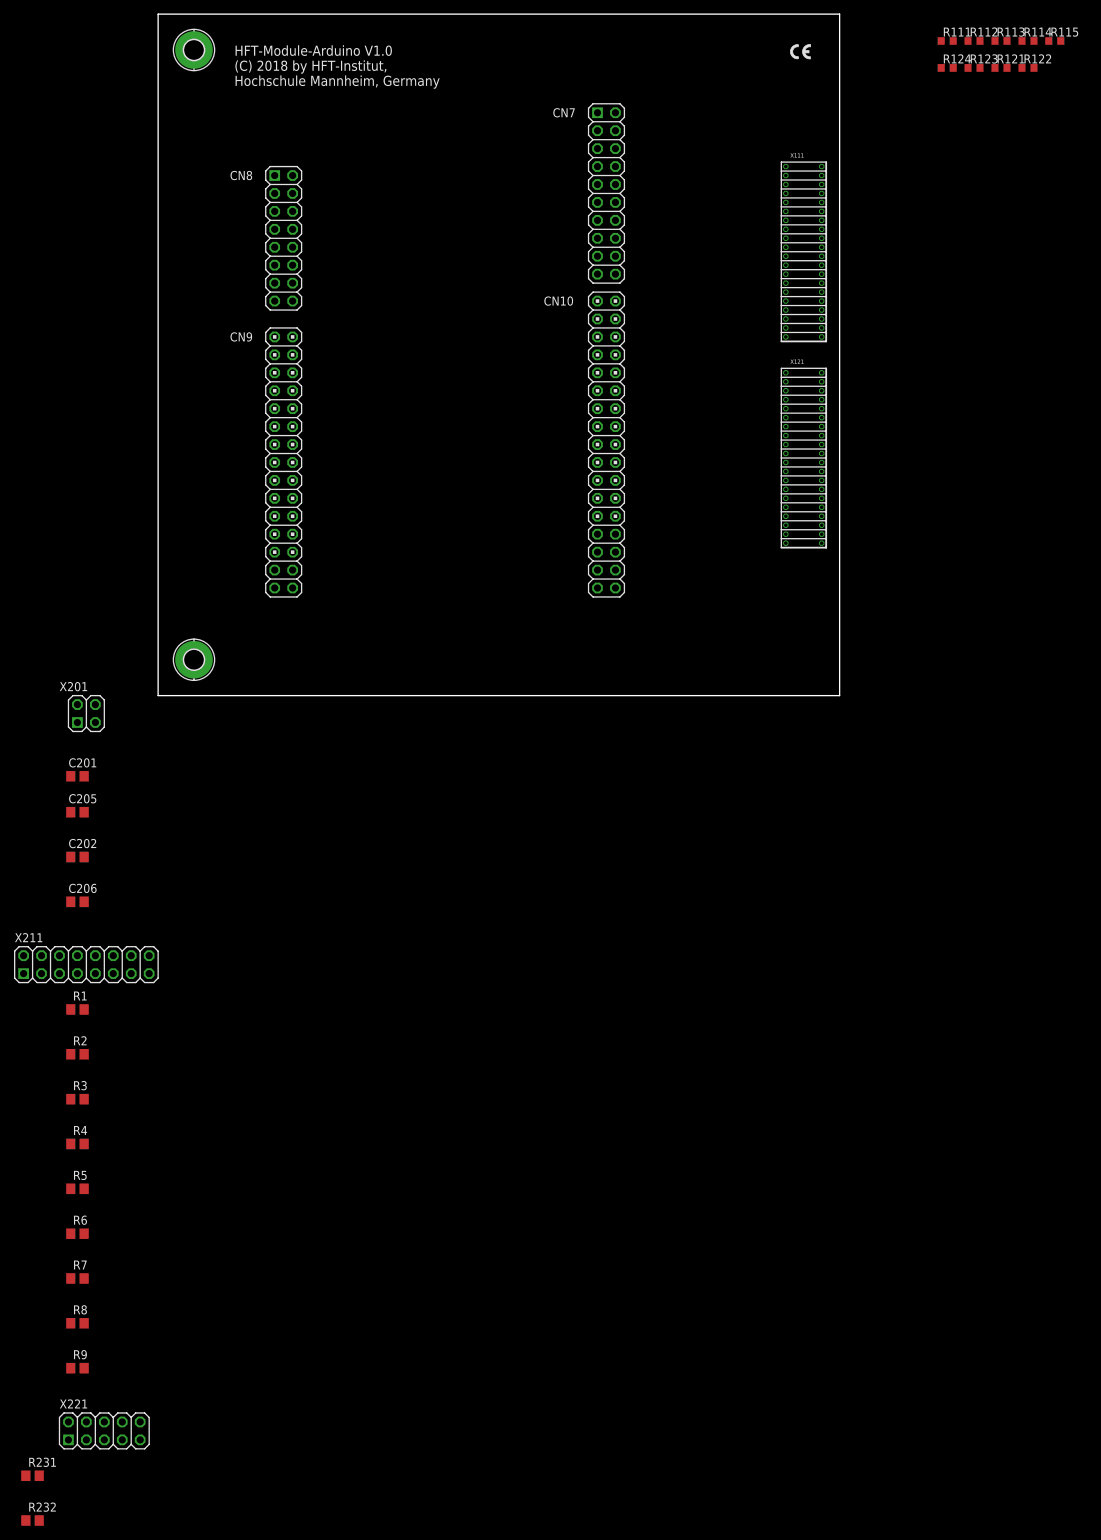
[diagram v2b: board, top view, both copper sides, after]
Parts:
- added C201, C205: 100nF, rcl:C0805
- added C202, C206: 1uF, rcl:C0805
- added CN10: (no value), df4iah_connector:2X17
- added CN7: (no value), df4iah_connector:2X10
- added CN8, X211: (no value), df4iah_connector:2X08
- added CN9: (no value), df4iah_connector:2X15
- added R1, R2, R3, R4, R5, R6, R7, R8, R9: 0R, rcl:R0805
- added R231, R232: 3k3R, rcl:R0805
- added X201: (no value), df4iah_connector:2X02
- added X221: (no value), df4iah_connector:2X05
- moved R111 41.6 mm to (111.8, 92.7)
- moved R113 41.6 mm to (119.4, 92.7)
- moved R114 41.6 mm to (123.2, 92.7)
- moved R115 41.6 mm to (127.0, 92.7)
- moved R121 41.6 mm to (119.4, 88.9)
- moved R122 41.6 mm to (123.2, 88.9)
- moved R124 41.6 mm to (111.8, 88.9)
- moved R112 41.6 mm to (115.6, 92.7)
- moved R123 41.6 mm to (115.6, 88.9)
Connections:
- removed net EXP_PX1__INOUT: X121.31
- new net A0: CN9.1
- new net A1: CN9.3
- new net A2: CN9.5
- new net A3: CN9.7
- new net A4_SDA: CN7.4, CN9.9, R4.2, R6.1
- new net A5_SCL: CN7.2, CN9.11, R3.2, R5.1
- new net AREF: CN7.6
- new net D0_RX: CN10.16, R1.1
- new net D10_SS: CN7.16, X221.1, X221.3, X221.5, X221.7, X221.9
- new net D11_MOSI: CN7.14, R9.1
- new net D12_MISO: CN7.12, R8.1
- new net D13_SCK: CN7.10, R7.1
- new net D1_TX: CN10.14, R2.1
- new net D2_INT0: CN10.12
- new net D3_INT1: CN10.10
- new net D4_T0: CN10.8
- new net D5_T1: CN10.6
- new net D6: CN10.4
- new net D7: CN10.2
- new net D8: CN7.20
- new net D9: CN7.18
- new net EXP_PX1_INOUT: X121.31, X211.12, X221.6
- new net IOREF: CN8.3, X201.1, X201.3
- new net NRST: CN8.5, X211.1, X211.11, X211.13, X211.15, X211.3, X211.5, X211.7, X211.9
- new net VIN: CN8.15
- net +3V3: now also C201.1, C202.1, CN8.7, R231.2, R232.2, X201.4
- net +5V0: now also C205.1, C206.1, CN8.9, X201.2
- net EXP_EVENT_IN: now also X211.6
- net EXP_I2C_SCL_IN: now also R232.1, R3.1, R5.2
- net EXP_I2C_SDA_INOUT: now also R231.1, R4.1, R6.2
- net EXP_PX0_INOUT: now also X211.14, X221.8
- net EXP_PX2_INOUT: now also X211.10, X221.4
- net EXP_PX3_INOUT: now also X211.8, X221.2
- net EXP_TMRCAPT_OUT: now also X211.4
- net EXP_UART_RX_IN: now also R2.2
- net EXP_UART_TX_OUT: now also R1.2
- net EXP_WAKEUP_OUT: now also X211.2
- net GND: now also C201.2, C202.2, C205.2, C206.2, CN7.8, CN8.11, CN8.13

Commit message: HW_1V0 - CAD/Eagle - components placed first round
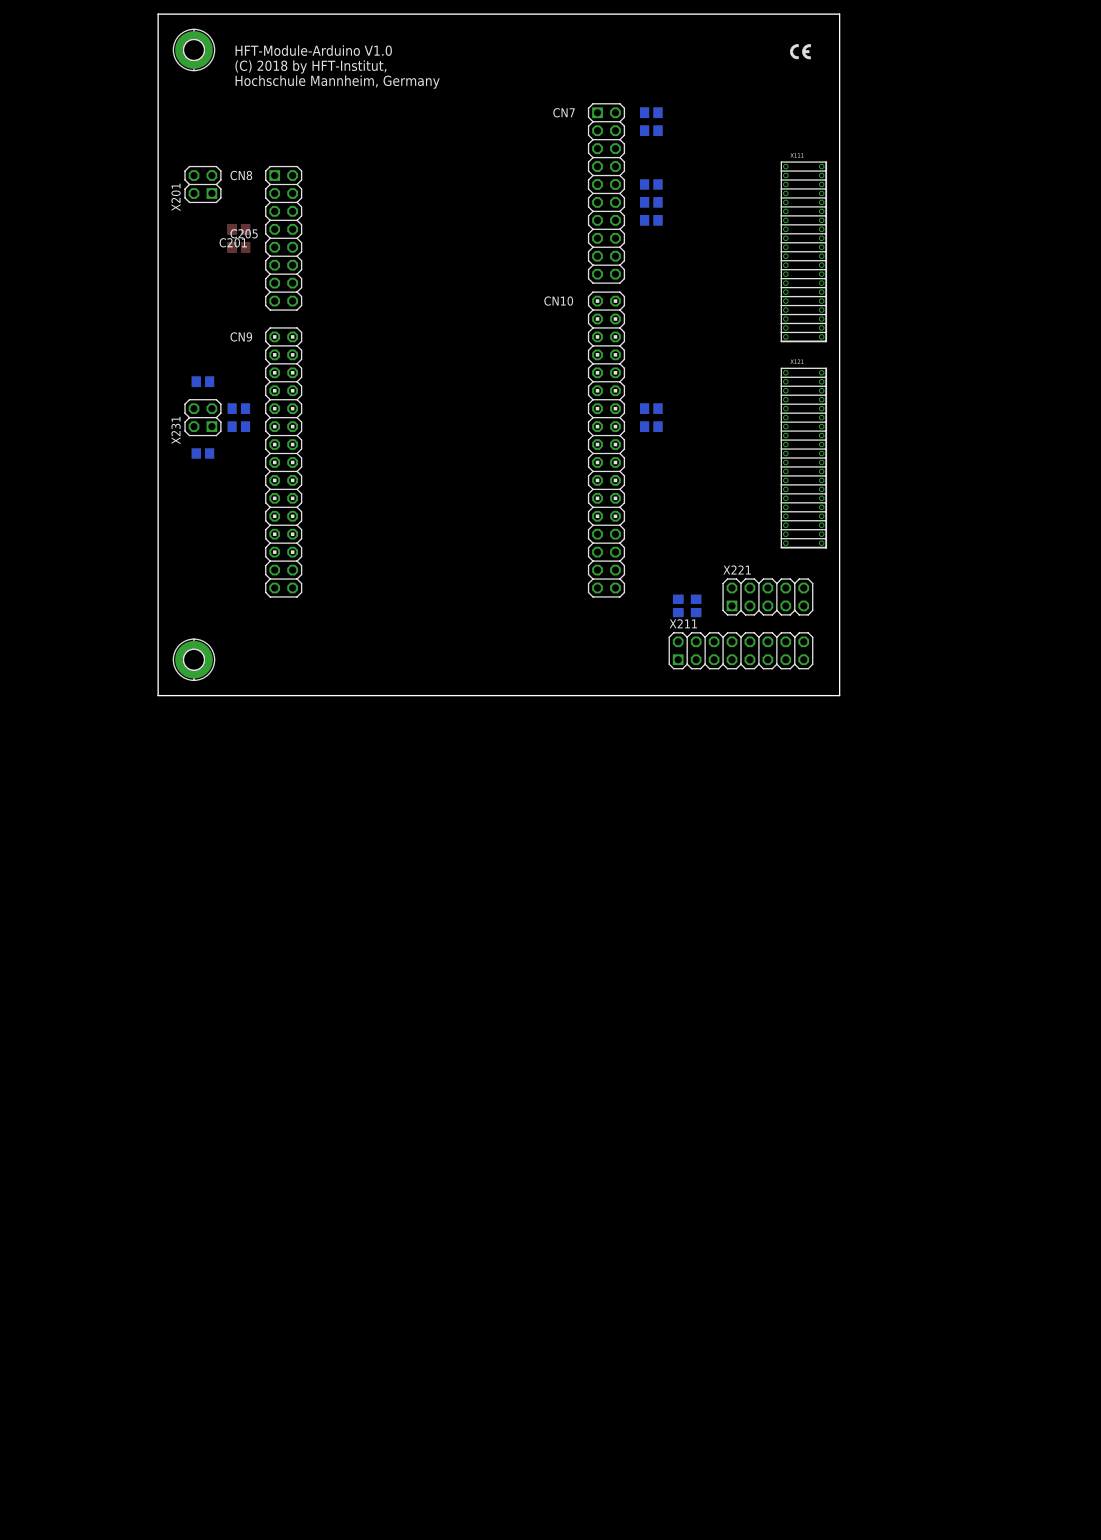
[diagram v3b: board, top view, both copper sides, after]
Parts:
- removed R1, R2, R3, R4, R5, R6, R7, R8, R9: 0R, rcl:R0805
- removed R111, R112, R113, R114, R123: 47R, rcl:R0603
- added R311, R312, R313, R314, R321, R323, R331: 0R, rcl:R0805
- added X231: (no value), df4iah_connector:2X02
- R115, R121, R122, R124: device rcl:R0603 -> rcl:R0805
- moved R232 163.1 mm to (6.35, 44.5), flipped to the bottom, turned to 180 degrees
- moved X221 150.9 mm to (86.4, 14.0)
- moved R231 146.8 mm to (6.35, 34.3), flipped to the bottom, turned to 180 degrees
- moved X211 102.8 mm to (82.5, 6.35)
- moved C206 95.5 mm to (11.4, 63.5), flipped to the bottom, turned to 180 degrees
- moved C202 91.8 mm to (11.4, 66.0), flipped to the bottom
- moved R122 89.5 mm to (76.2, 12.7), flipped to the bottom, turned to 90 degrees
- moved R121 88.9 mm to (73.7, 12.7), flipped to the bottom, turned to 90 degrees
- moved C205 83.2 mm to (11.4, 63.5)
- moved C201 80.8 mm to (11.4, 66.0), turned to 180 degrees
- moved X201 76.7 mm to (6.35, 72.4), turned to 90 degrees
- moved R124 65.9 mm to (69.8, 38.1), flipped to the bottom, turned to 180 degrees
- moved R115 61.6 mm to (69.8, 69.8), flipped to the bottom, turned to 180 degrees
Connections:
- removed net EXP_I2S_MSR_FS_OUT: R112.1
- removed net EXP_I2S_MSR_MCLK_OUT: R111.1
- removed net EXP_I2S_MSR_SCK_OUT: R113.1
- removed net EXP_I2S_MSR_SD_OUT: R114.1
- removed net EXP_SPI_MISO_OUT: R115.1
- removed net EXP_UART_RTS_OUT: R123.1
- removed net EXP_UART_TX_OUT: R1.2, R124.1
- new net N$1: R231.1, X231.2
- new net N$2: R232.1, X231.4
- net A4_SDA: now also R311.2, R314.1; no longer R4.2, R6.1
- net A5_SCL: now also R312.2, R313.1; no longer R3.2, R5.1
- net D0_RX: now also R124.1; no longer R1.1
- net D11_MOSI: now also R323.1; no longer R9.1
- net D12_MISO: now also R115.1; no longer R8.1
- net D13_SCK: now also R321.1; no longer R7.1
- net D1_TX: now also R331.1; no longer R2.1
- net EXP_I2C_SCL_IN: now also R312.1, R313.2, X231.3; no longer R232.1, R3.1, R5.2
- net EXP_I2C_SDA_INOUT: now also R311.1, R314.2, X231.1; no longer R231.1, R4.1, R6.2
- net EXP_I2S_MSR_FS_OUT_R: no longer R112.2
- net EXP_I2S_MSR_MCLK_OUT_R: no longer R111.2
- net EXP_I2S_MSR_SCK_OUT_R: no longer R113.2
- net EXP_I2S_MSR_SD_OUT_R: no longer R114.2
- net EXP_SPI_MOSI_IN: now also R323.2
- net EXP_SPI_SCK_IN: now also R321.2
- net EXP_UART_RTS_OUT_R: no longer R123.2
- net EXP_UART_RX_IN: now also R331.2; no longer R2.2
